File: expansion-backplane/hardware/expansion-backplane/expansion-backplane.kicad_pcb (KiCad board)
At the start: 2 copper layers, 119 x 51 mm, 26 parts, among them J1 Barrel_Jack, SW1 SW_SPDT, U1 74AHCT126

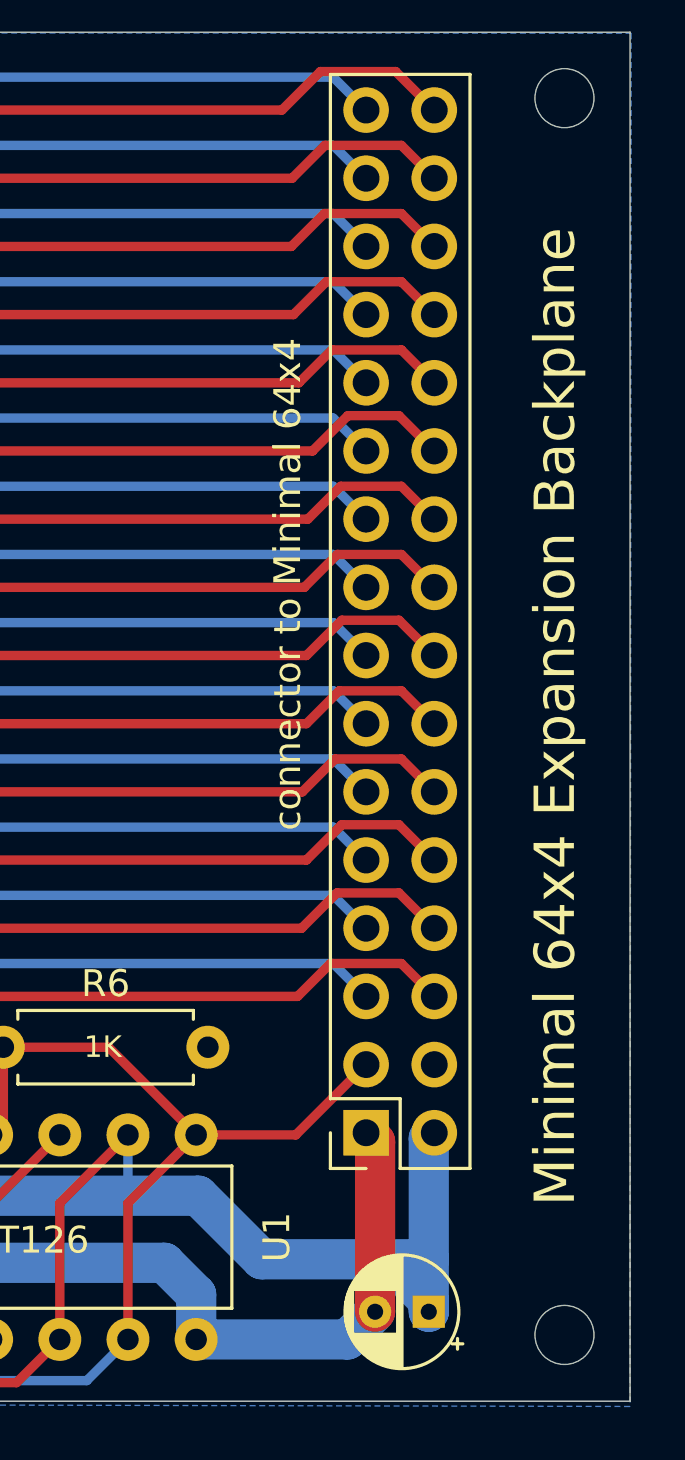
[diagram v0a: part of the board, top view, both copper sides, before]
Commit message: first version of multiplier board
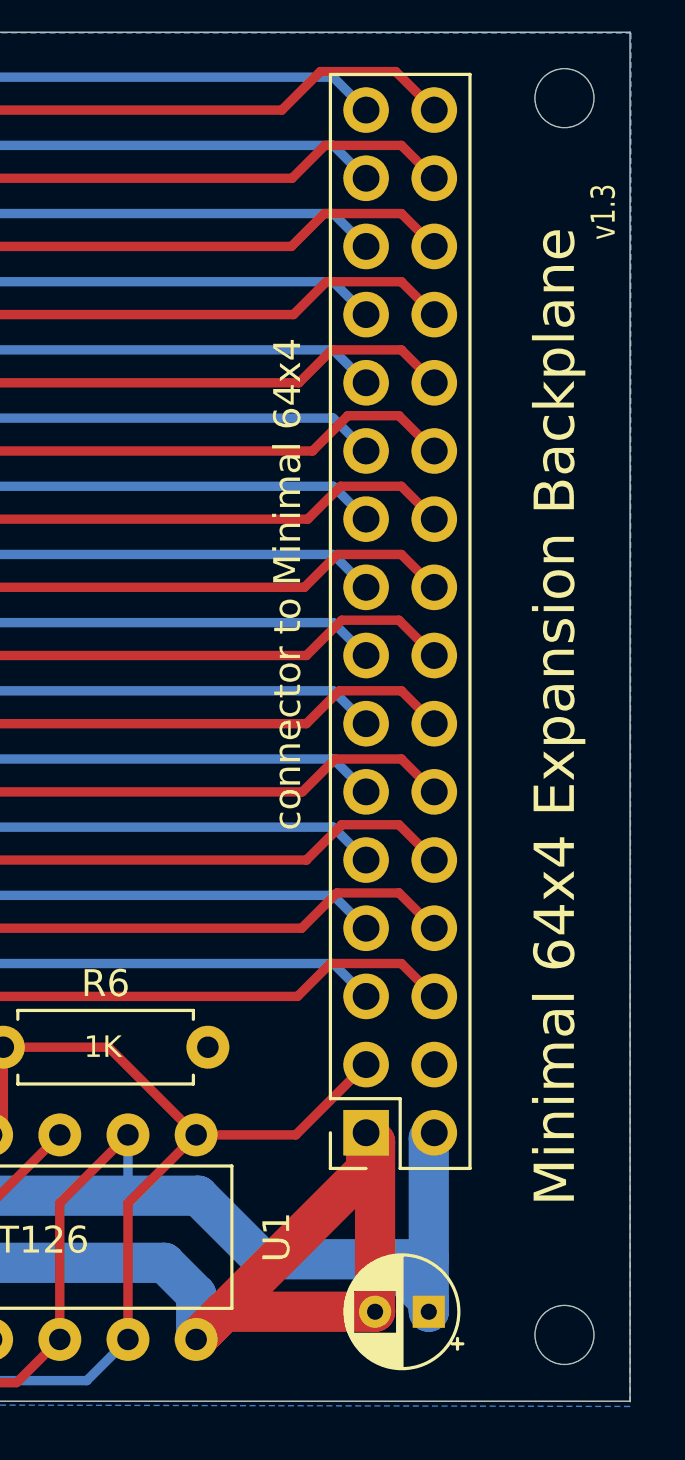
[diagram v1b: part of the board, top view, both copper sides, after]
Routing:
- net GND: track 185.5 -> 195.8 mm
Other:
- board text added: "v1.3"
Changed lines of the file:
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@@
 			(drillshape 0)
 			(scaleselection 1)
-			(outputdirectory "gerbers_v1.2")
+			(outputdirectory "gerbers_v1.3")
 		)
 	)
@@
 		)
 	)
+	(gr_text "v1.3"
+		(at 213.5378 97.7392 90)
+		(layer "F.SilkS")
+		(effects
+			(font
+				(size 0.9 0.7)
+				(thickness 0.1)
+			)
+			(justify left bottom)
+		)
+	)
 	(gr_text "A7"
 		(at 158.054645 105.41 0)
@@
 	)
 	(segment
+		(start 204.166645 132.368355)
+		(end 197.8356 138.6994)
+		(width 1.5)
+		(layer "F.Cu")
+		(net 1)
+	)
+	(segment
+		(start 204.502 137.668)
+		(end 198.867 137.668)
+		(width 1.5)
+		(layer "F.Cu")
+		(net 1)
+	)
+	(segment
+		(start 198.867 137.668)
+		(end 197.8356 138.6994)
+		(width 1.5)
+		(layer "F.Cu")
+		(net 1)
+	)
+	(segment
 		(start 204.502 137.668)
 		(end 204.502 131.335355)
@@
 	)
 	(segment
+		(start 204.166645 131)
+		(end 204.166645 132.368355)
+		(width 1.5)
+		(layer "F.Cu")
+		(net 1)
+	)
+	(segment
 		(start 117.206645 131)
 		(end 117.206645 137.644)
@@
 	)
 	(segment
-		(start 203.4706 138.6994)
-		(end 204.502 137.668)
-		(width 1.5)
-		(layer "B.Cu")
-		(net 1)
-	)
-	(segment
 		(start 135.230645 139.243845)
 		(end 135.382 139.3952)
@@
 		(width 1.5)
 		(layer "B.Cu")
-		(net 1)
-	)
-	(segment
-		(start 197.8356 138.6994)
-		(end 203.4706 138.6994)
-		(width 1.5)
-		(layer "B.Cu")

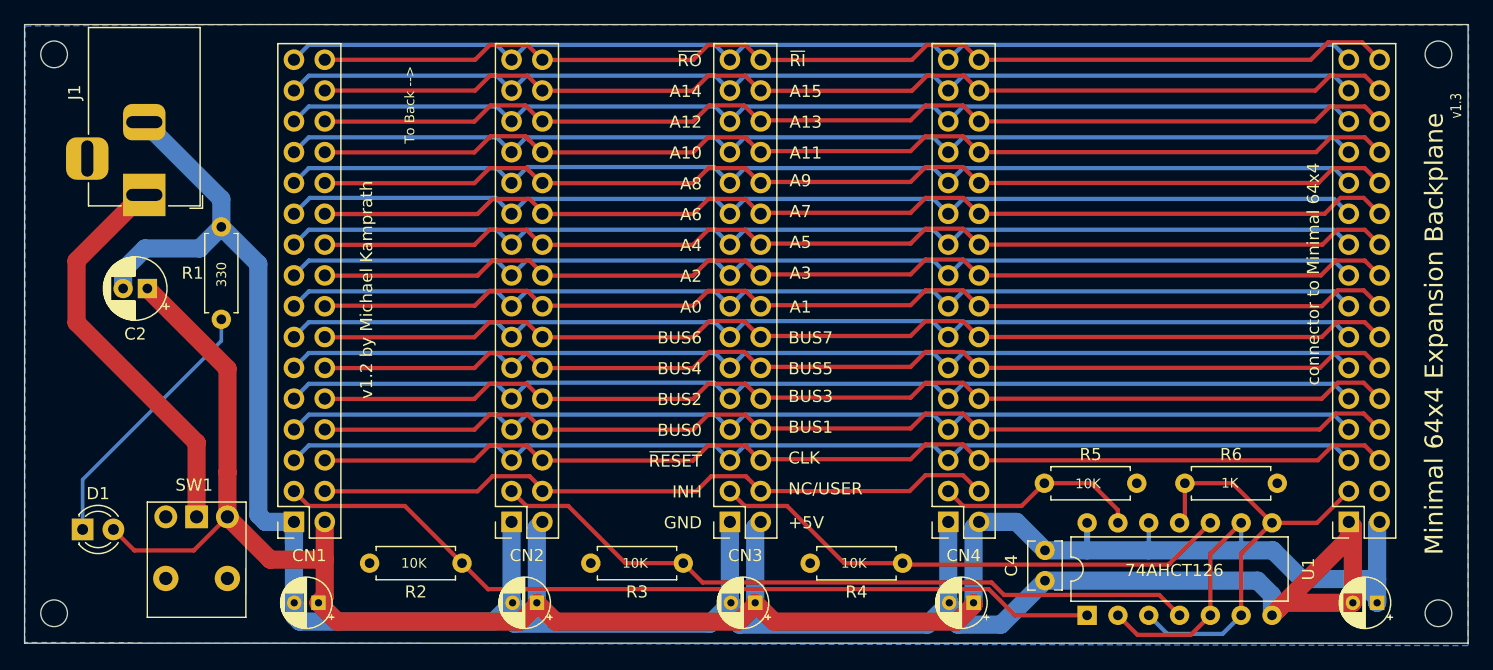
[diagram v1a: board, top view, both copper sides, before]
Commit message: added better ground plane
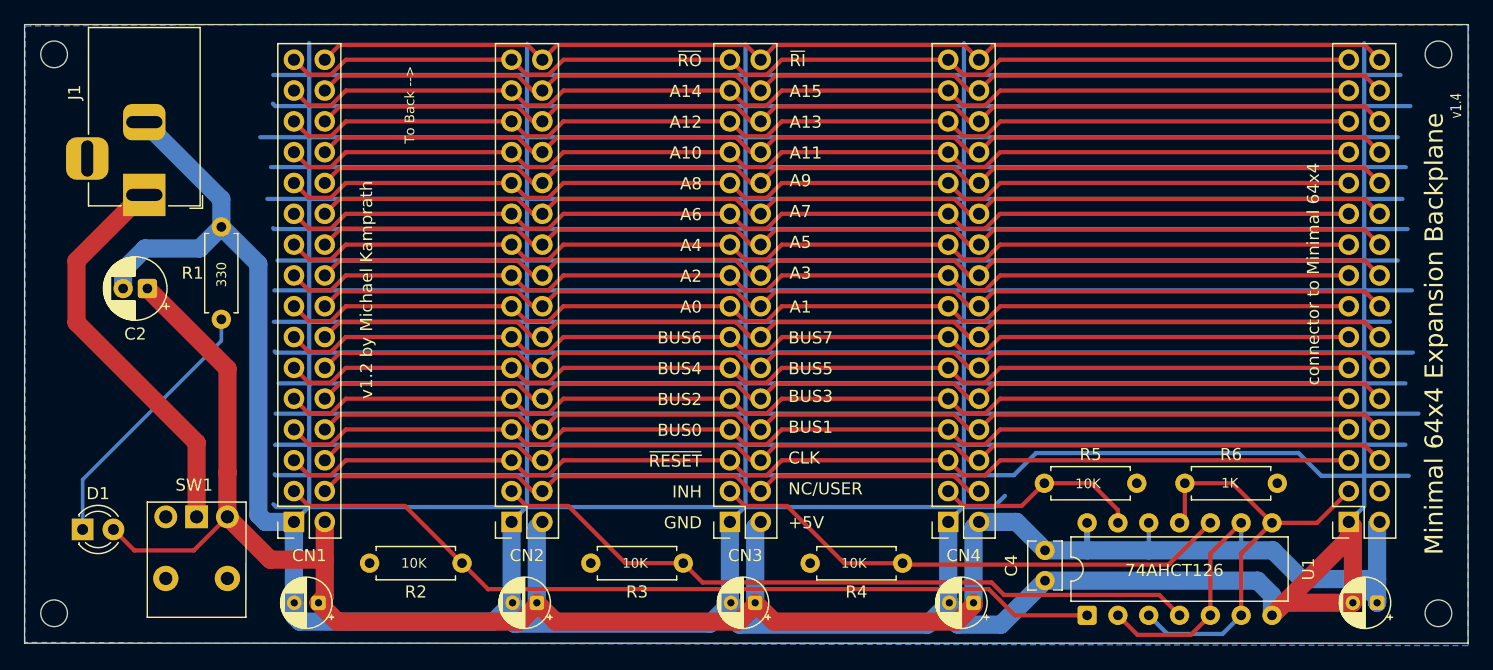
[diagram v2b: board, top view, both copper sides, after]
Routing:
- net GND: track 195.8 -> 1765.1 mm
- net A11: track 91.6 -> 91.0 mm
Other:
- board text added: "v1.4"
- board text removed: "v1.3"
